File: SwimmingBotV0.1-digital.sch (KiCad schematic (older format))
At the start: 12 parts

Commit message: woohoo getting there
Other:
- note added: "REV2 QUESTION: DO I REALLY NEED PARALLEL FLASH?"
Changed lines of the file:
@@
 Text Notes 5950 5200 0    60   ~ 0
 Flash
+Text Notes 900  750  0    200  ~ 0
+REV2 QUESTION:  DO I REALLY NEED PARALLEL FLASH?
 $EndSCHEMATC

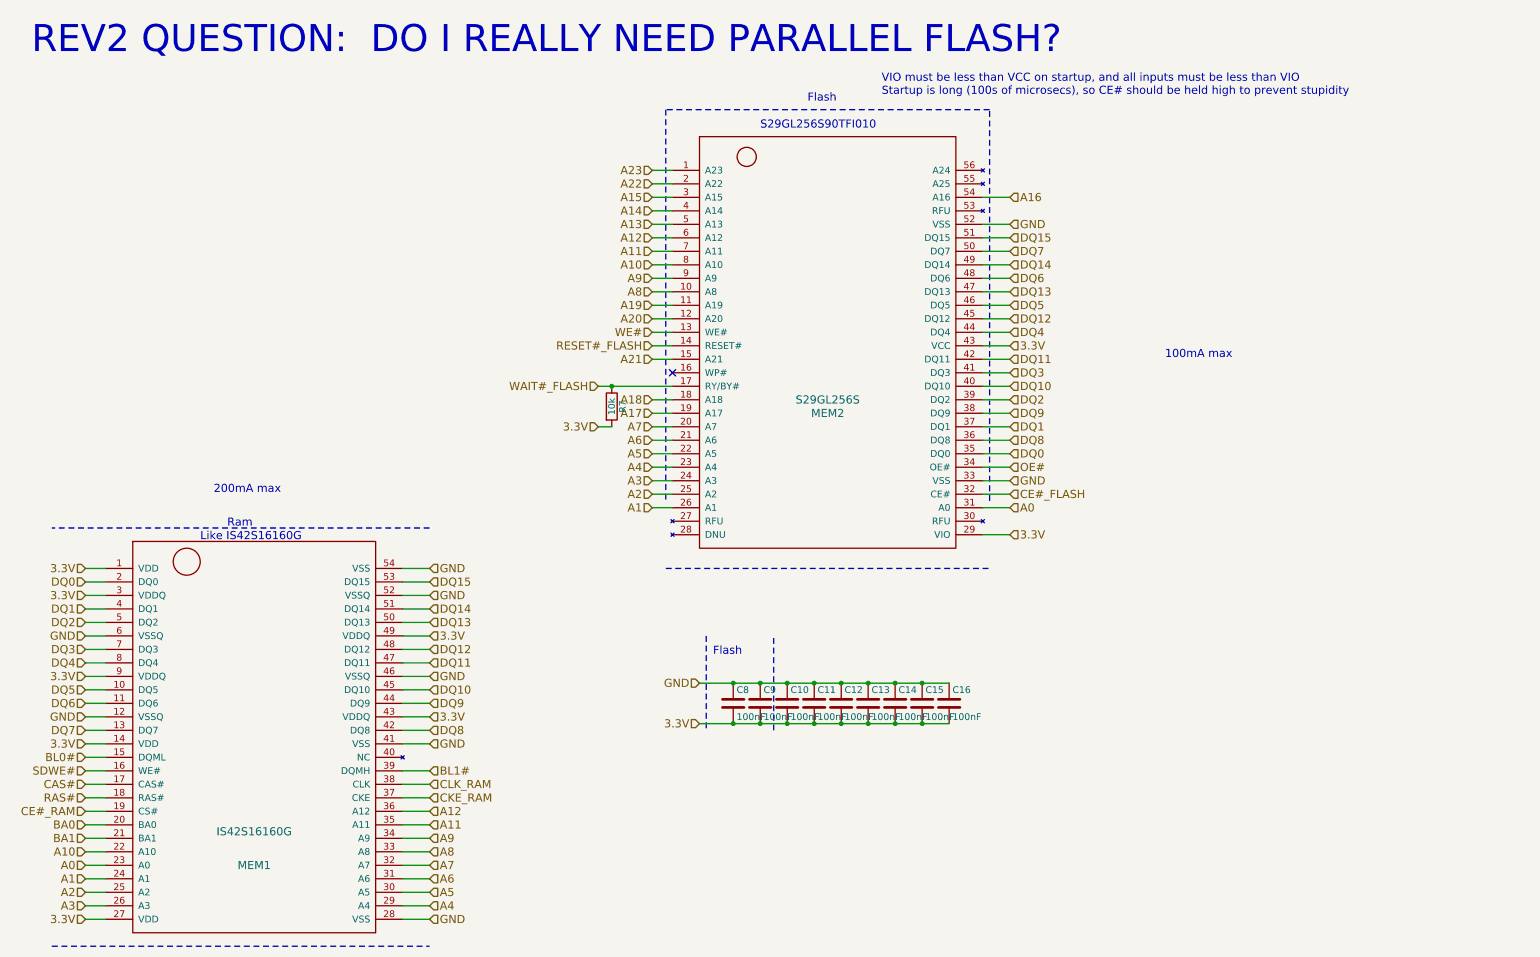
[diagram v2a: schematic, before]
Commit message: removed old ram and flash, added new flash, switched to 100 pin micro
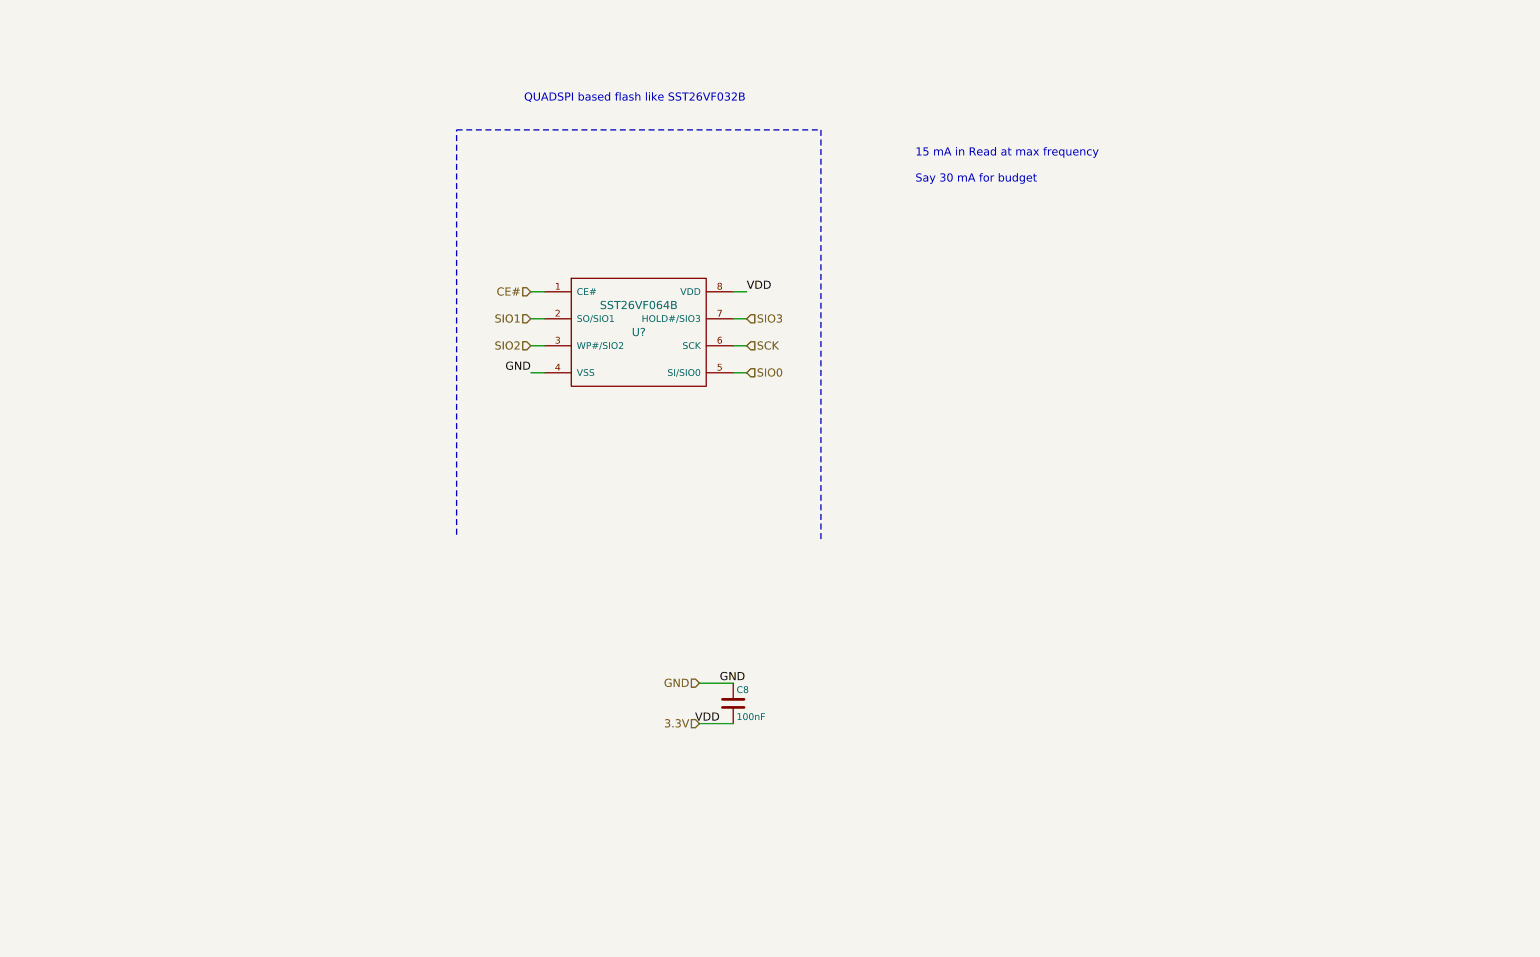
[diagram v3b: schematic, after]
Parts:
- removed C10, C11, C12, C13, C14, C15, C16, C9: 100nF, Capacitors_SMD:C_0402, symbol C
- removed MEM1: IS42S16160G, Custom_Footprints:TSOP-54, symbol IS42S16160G
- removed MEM2: S29GL256S, Custom_Footprints:TSOP-56_TYPE_1, symbol S29GL256S
- removed R7: 10k, Resistors_SMD:R_0402, symbol R
- added U?: SST26VF064B, symbol SST26VF064B
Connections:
- net 3.3V: now also U?.8 (VDD)
- net GND: now also U?.4 (VSS)
- new net CE#: U?.1 (CE#)
- new net SCK: U?.6 (SCK)
- new net SIO0: U?.5 (SI/SIO0)
- new net SIO1: U?.2 (SO/SIO1)
- new net SIO2: U?.3 (WP#/SIO2)
- new net SIO3: U?.7 (HOLD#/SIO3)
- no-connect marks 1 -> 0
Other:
- note added: "15 mA in Read at max frequency\n\nSay 30 mA for budget"
- note added: "QUADSPI based flash like SST26VF032B"
- note removed: "100mA max"
- note removed: "200mA max"
- note removed: "Flash"
- note removed: "Like IS42S16160G"
- note removed: "REV2 QUESTION: DO I REALLY NEED PARALLEL FLASH?"
- note removed: "Ram"
- note removed: "S29GL256S90TFI010"
- note removed: "VIO must be less than VCC on startup, and all inputs must be less than VIO\nStartup is long (100s of microsecs), so CE# should be held high to prevent stupidity"

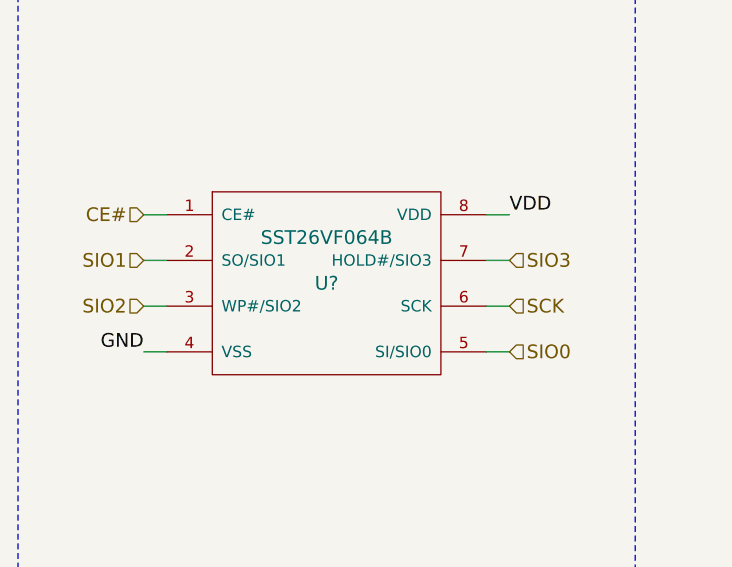
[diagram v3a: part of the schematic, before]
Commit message: potentially done with parts removal and reselection, on to pcb layout
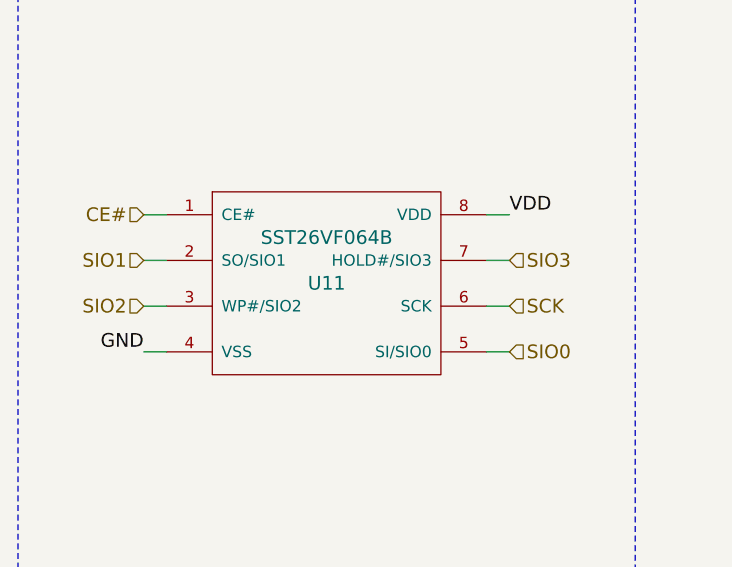
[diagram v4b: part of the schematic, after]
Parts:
- gave numbers to parts that had none: 1
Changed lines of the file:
@@
 	5850 5700 6100 5700
 $Comp
-L SST26VF064B U?
+L SST26VF064B U11
 U 1 1 5792453C
 P 5400 3000
-F 0 "U?" H 5400 3200 60  0000 C CNN
+F 0 "U11" H 5400 3200 60  0000 C CNN
 F 1 "SST26VF064B" H 5400 3400 60  0000 C CNN
 F 2 "" H 5400 3000 60  0000 C CNN

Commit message: pcb started in earnest, footprint changes in schematics, about to rename v0.2 boardfile to v0.1, kicad needs the same filename to have backrefs for net highlighting
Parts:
- U11: footprint (none) -> Housings_SOIC:SOIJ-8_5.3x5.3mm_Pitch1.27mm
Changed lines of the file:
@@
 F 0 "U11" H 5400 3200 60  0000 C CNN
 F 1 "SST26VF064B" H 5400 3400 60  0000 C CNN
-F 2 "" H 5400 3000 60  0000 C CNN
+F 2 "Housings_SOIC:SOIJ-8_5.3x5.3mm_Pitch1.27mm" H 5400 3000 60  0001 C CNN
 F 3 "" H 5400 3000 60  0000 C CNN
 	1    5400 3000
